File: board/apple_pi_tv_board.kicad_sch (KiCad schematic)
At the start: 5 parts, among them U3 RPi_4

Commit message: updated most stuff, but i completely redid the diff pairs
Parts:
- added D2, D3: LED_Small, LED_SMD:LED_0805_2012Metric, symbol Device:LED_Small
- added JP1-WL1, JP2-BT1, JP3-EEPROM1: SolderJumper_2_Open, Jumper:SolderJumper-2_P1.3mm_Open_TrianglePad1.0x1.5mm, symbol Jumper:SolderJumper_2_Open
- added R9: R, Resistor_SMD:R_0402_1005Metric, symbol Device:R
- added TP1: RUN_PG, TestPoint:TestPoint_Pad_D1.5mm, symbol Connector:TestPoint
- added TP2: Extrst, TestPoint:TestPoint_Pad_D1.5mm, symbol Connector:TestPoint
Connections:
- net +3V3: now also U3.78 (GPIO_VREF)
- net GND: now also D3.1 (K), JP1-WL1.1 (A), JP2-BT1.1 (A), JP3-EEPROM1.1 (A), R9.2
- net at U3.100 (~{EXTRST}): now also TP2.1
- net at U3.20 (EEPROM_~{WP}): now also JP3-EEPROM1.2 (B)
- net at U3.21 (PI_~{LED_ACTIVITY}): now also D3.2 (A)
- net at U3.89 (WL_~{DISABLE}): now also JP1-WL1.2 (B)
- net at U3.91 (BT_~{DISABLE}): now also JP2-BT1.2 (B)
- net at U3.92 (RUN_PG): now also TP1.1
- net at U3.95 (PI_LED_~{PWR}): now also D2.2 (A)
- new net: D2.1 (K), R9.1

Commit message: almost v0.3
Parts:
- U3: now left out of the parts list
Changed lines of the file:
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@@
 		(unit 1)
 		(exclude_from_sim no)
-		(in_bom yes)
+		(in_bom no)
 		(on_board yes)
 		(dnp no)
@@
 		(unit 2)
 		(exclude_from_sim no)
-		(in_bom yes)
-		(on_board yes)
-		(dnp no)
+		(in_bom no)
+		(on_board yes)
+		(dnp no)

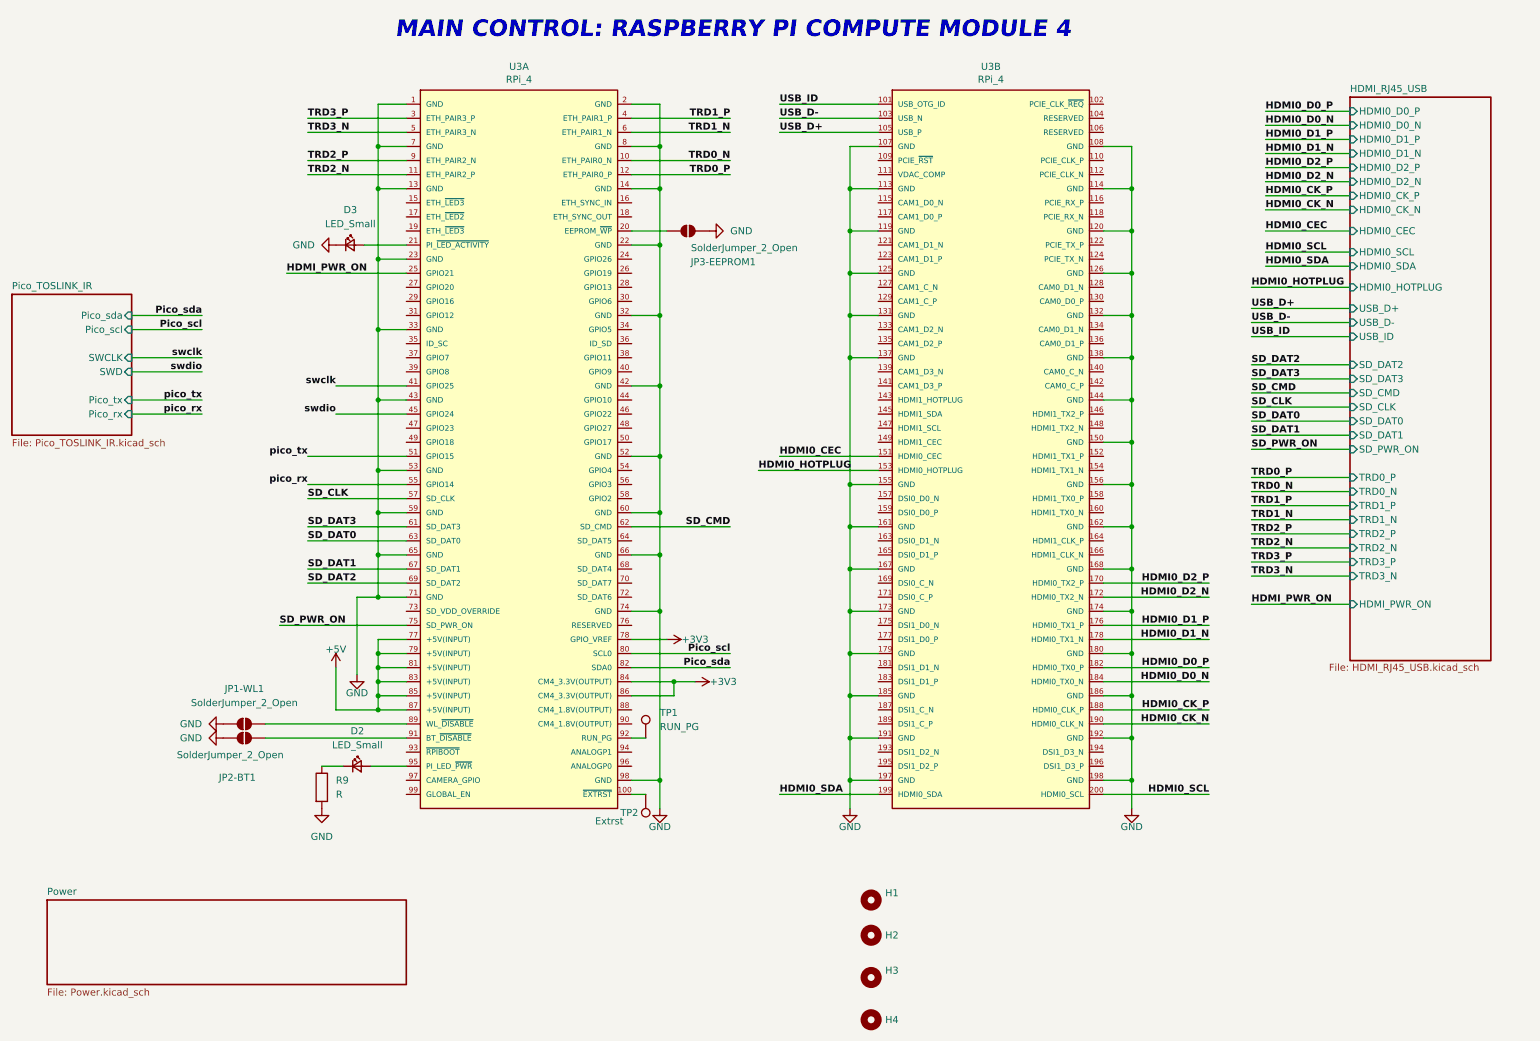
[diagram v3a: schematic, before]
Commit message: going to add the magnetic transformer which will messs a lot of stuff up
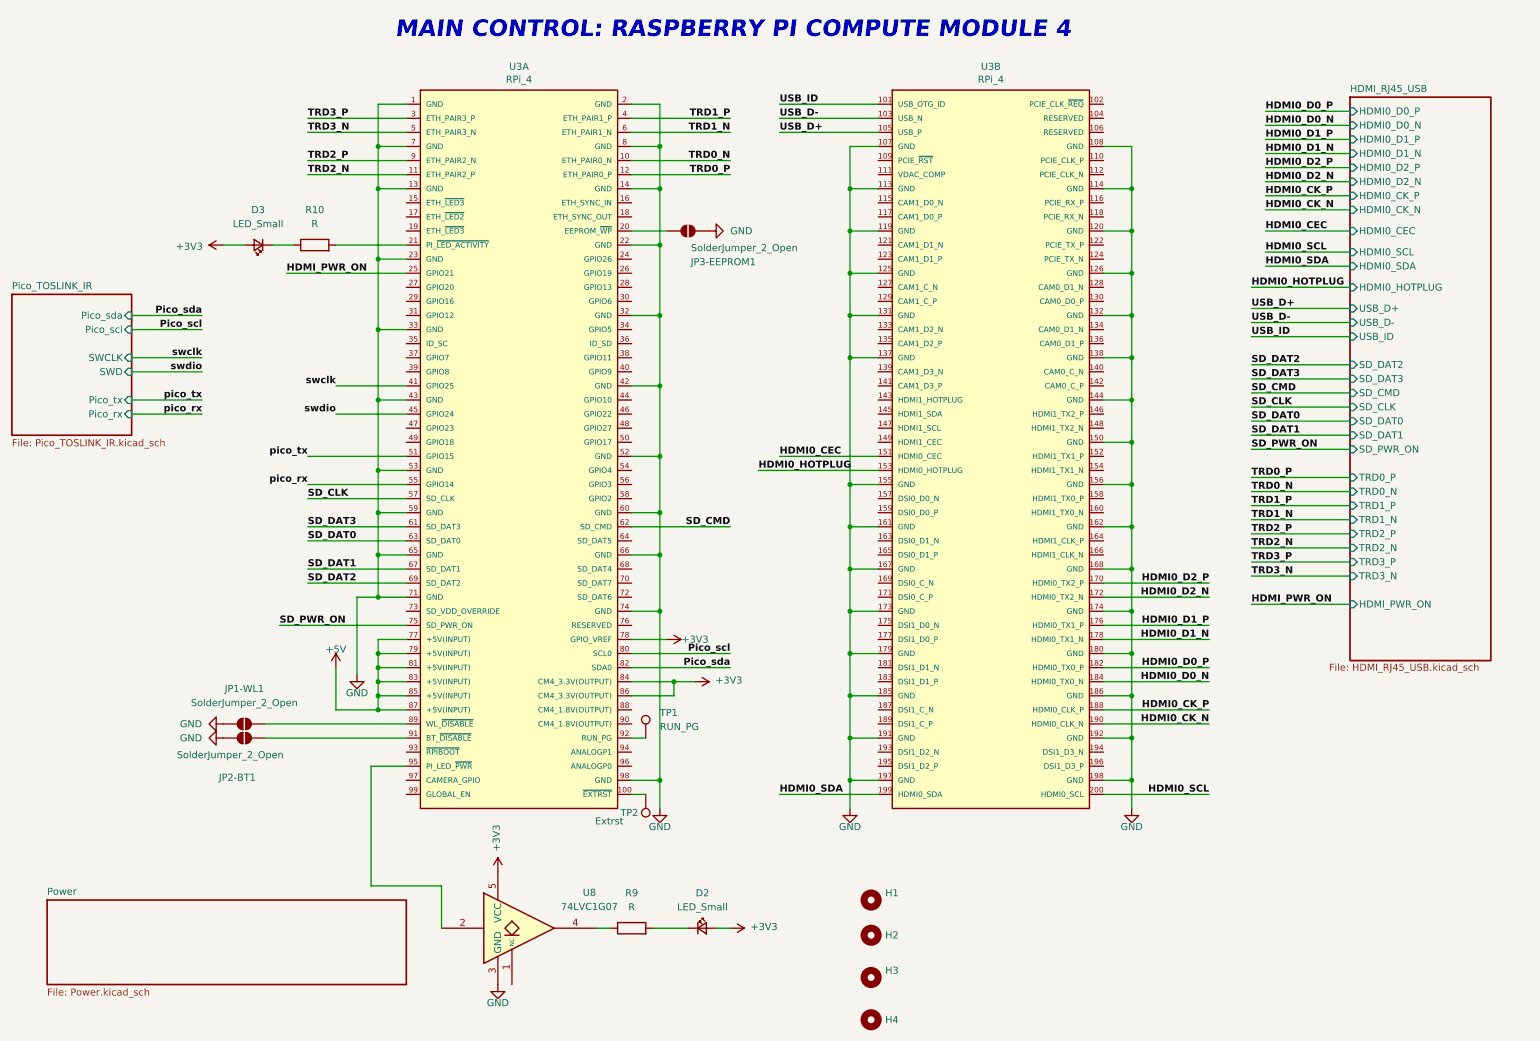
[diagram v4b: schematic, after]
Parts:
- added R10: R, Resistor_SMD:R_0402_1005Metric, symbol Device:R
- added U8: 74LVC1G07, Package_TO_SOT_SMD:SOT-23-5, symbol 74xGxx:74LVC1G07
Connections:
- net +3V3: now also D2.2 (A), D3.2 (A), U8.5 (VCC)
- net GND: now also U8.3 (GND); no longer D3.1 (K), R9.2
- net at U3.21 (PI_~{LED_ACTIVITY}): now also R10.2; no longer D3.2 (A)
- net at U3.95 (PI_LED_~{PWR}): now also U8.2; no longer D2.2 (A)
- net at R9.1: now also U8.4; no longer D2.1 (K)
- new net: D3.1 (K), R10.1
- new net: D2.1 (K), R9.2
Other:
- moved on the sheet: D2, D3, R9

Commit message: started more ethernet adding stuff
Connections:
- net TRD2_N: now also U3.9 (ETH_PAIR2_N); no longer U3.11 (ETH_PAIR2_P)
- net TRD2_P: now also U3.11 (ETH_PAIR2_P); no longer U3.9 (ETH_PAIR2_N)
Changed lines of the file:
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@@
-		)
-	)
-	(label "TRD2_P"
-		(at 67.31 40.64 0)
-		(effects
-			(font
-				(size 1.27 1.27)
-				(bold yes)
-			)
-			(justify left bottom)
 		)
 	)
@@
 		)
 	)
-	(label "TRD2_N"
-		(at 67.31 43.18 0)
-		(effects
-			(font
-				(size 1.27 1.27)
-				(bold yes)
-			)
-			(justify left bottom)
-		)
-	)
 	(label "USB_D-"
 		(at 237.49 69.85 0)
@@
 		)
 	)
+	(label "TRD2_N"
+		(at 67.31 40.64 0)
+		(effects
+			(font
+				(size 1.27 1.27)
+				(bold yes)
+			)
+			(justify left bottom)
+		)
+	)
 	(label "HDMI0_CK_N"
 		(at 240.03 49.53 0)
@@
 		(effects
 			(font
+				(size 1.27 1.27)
+				(bold yes)
+			)
+			(justify left bottom)
+		)
+	)
+	(label "TRD2_P"
+		(at 67.31 43.18 0)
+		(effects
+			(font

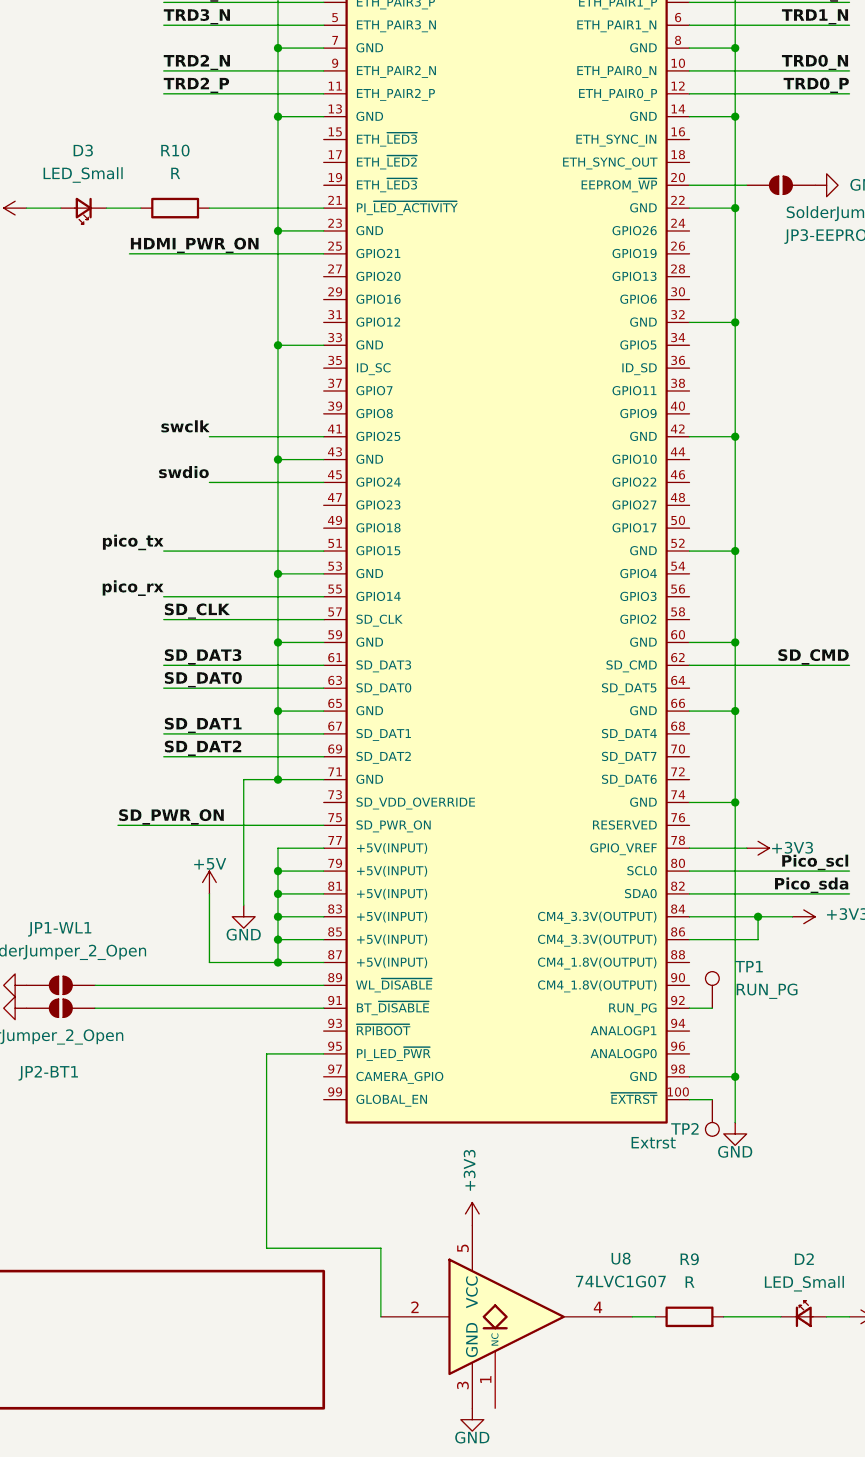
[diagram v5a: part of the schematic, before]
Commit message: removed some via's
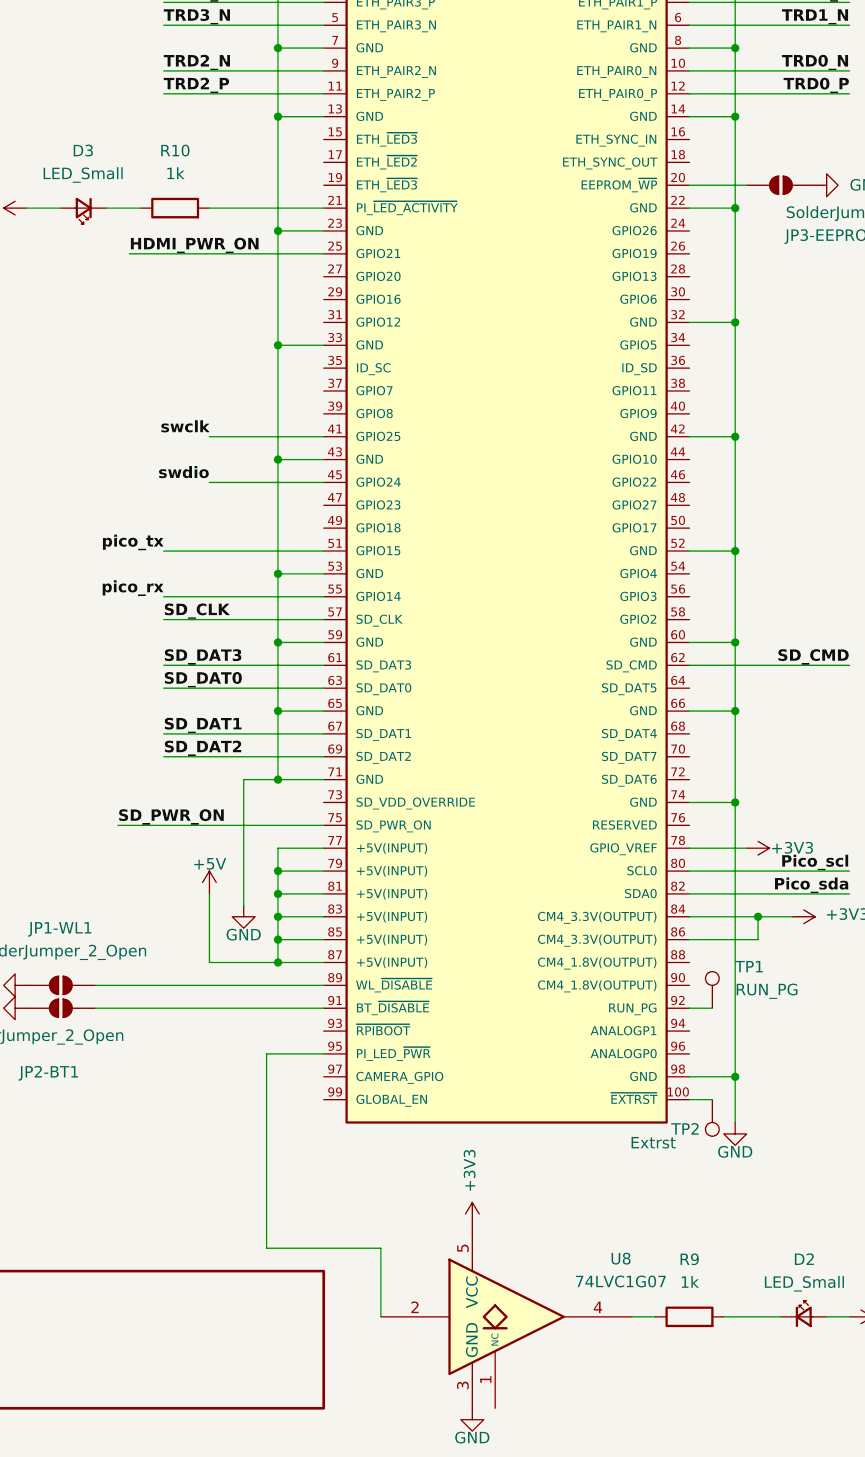
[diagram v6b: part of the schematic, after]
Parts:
- R10, R9: value R -> 1k
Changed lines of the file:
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@@
 			)
 		)
-		(property "Value" "R"
+		(property "Value" "1k"
 			(at 68.58 52.07 90)
 			(effects
@@
 			)
 		)
-		(property "Value" "R"
+		(property "Value" "1k"
 			(at 125.73 175.26 90)
 			(effects
